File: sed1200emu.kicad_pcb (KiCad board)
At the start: 2 copper layers, 46.2 x 38.9 mm, 17 parts, among them IC1 MEGA8-AI

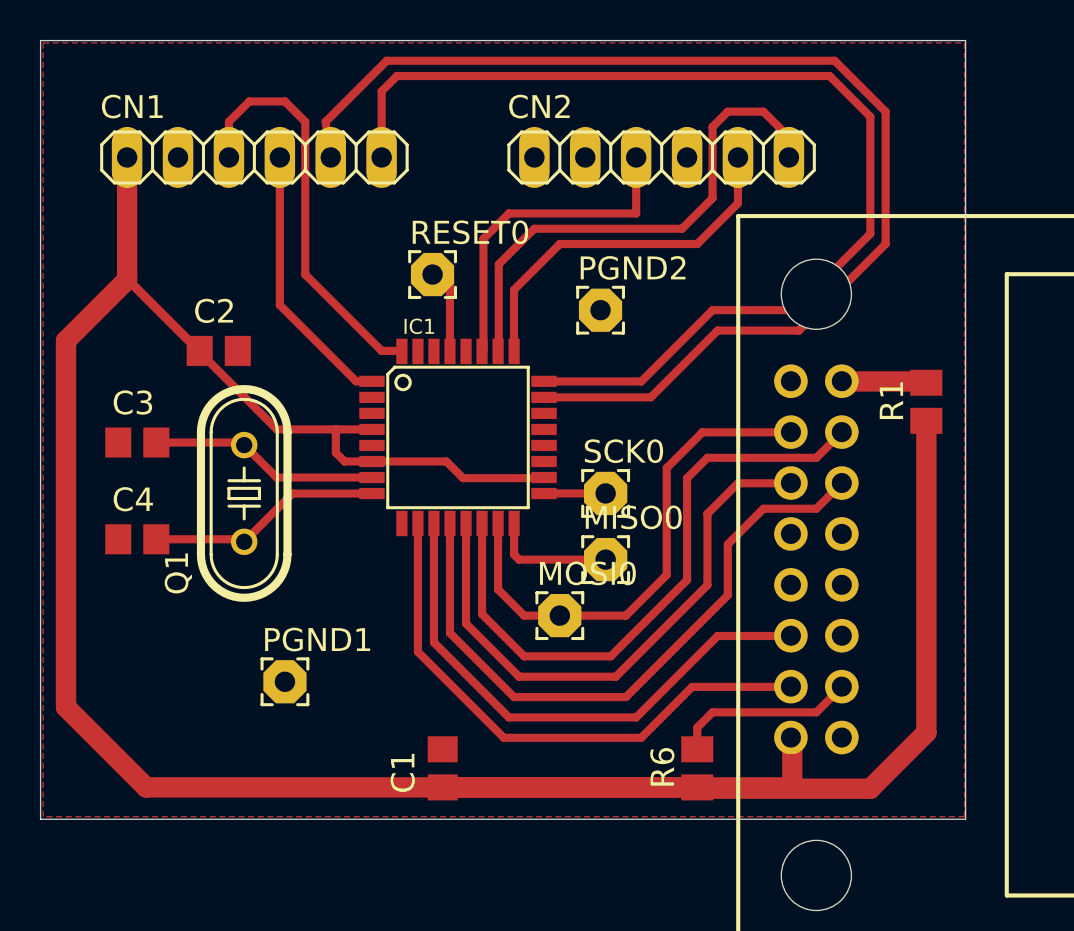
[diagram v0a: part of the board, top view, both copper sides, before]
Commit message: Replace MEGA8 Symbol and Footprint
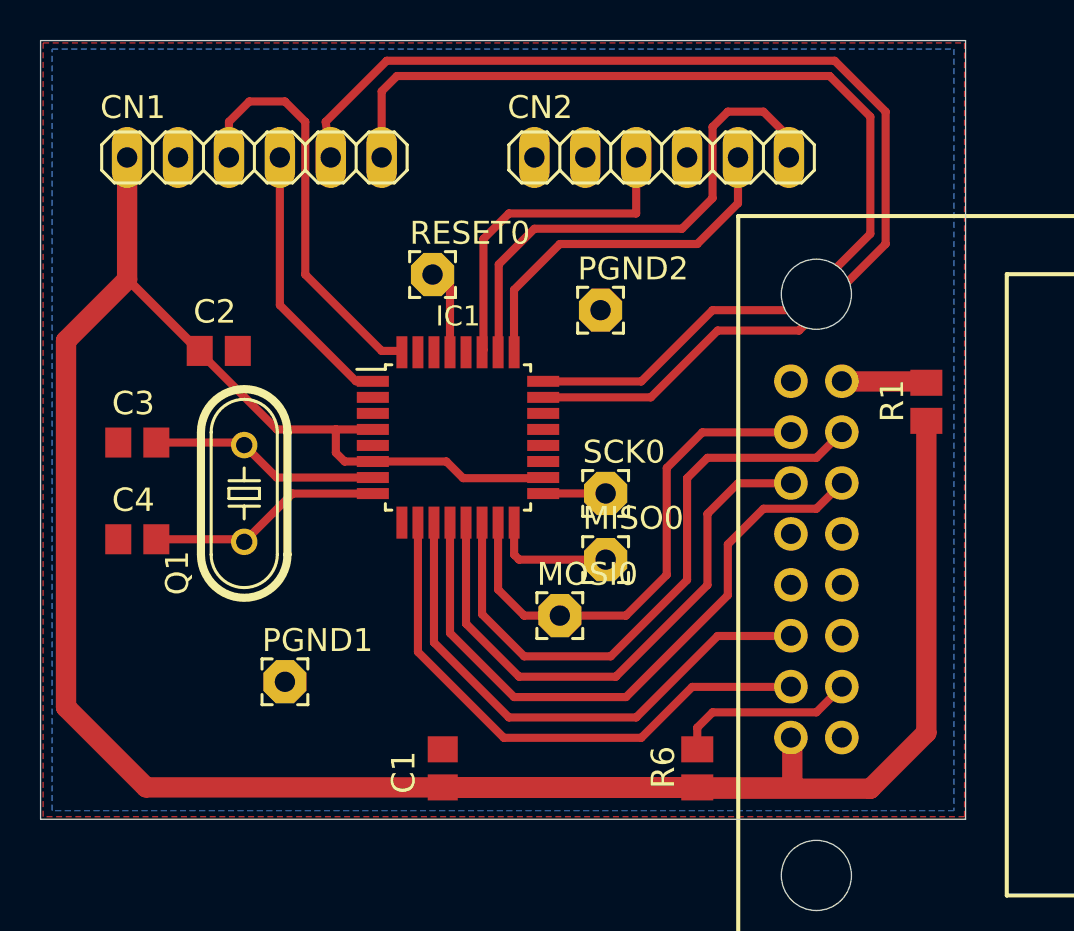
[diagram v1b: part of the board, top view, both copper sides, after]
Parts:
- CN1, CN2: value (none) -> PINHD-1X6
- IC1: footprint sed1200emu:TQFP32-08 -> Package_QFP:TQFP-32_7x7mm_P0.8mm
- PGND1, PGND2: value (none) -> 2,15/1,0
- Q1: value (none) -> CRYSTALHC49S
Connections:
- net PS2CLK renamed Net-(IC1-PD2(INT0))
- net PS2DATA renamed Net-(IC1-PD3(INT1))
- CN1 pad 2: (no net) -> unconnected-(CN1-Pad2)
- CN2 pad 2: (no net) -> unconnected-(CN2-Pad2)
- CN2 pad 4: (no net) -> unconnected-(CN2-Pad4)
- DIS2 pad 10: (no net) -> unconnected-(DIS2-D3-Pad10)
- DIS2 pad 15: N$7 -> unconnected-(DIS2-NC@1-Pad15)
- DIS2 pad 16: GND -> unconnected-(DIS2-NC@2-Pad16)
- DIS2 pad 7: (no net) -> unconnected-(DIS2-D0-Pad7)
- DIS2 pad 8: (no net) -> unconnected-(DIS2-D1-Pad8)
- DIS2 pad 9: (no net) -> unconnected-(DIS2-D2-Pad9)
- IC1 pad 19: (no net) -> unconnected-(IC1-ADC6-Pad19)
- IC1 pad 2: (no net) -> unconnected-(IC1-PD4(XCK/T0)-Pad2)
- IC1 pad 20: (no net) -> unconnected-(IC1-AREF-Pad20)
- IC1 pad 22: (no net) -> unconnected-(IC1-ADC7-Pad22)
- IC1 pad 28: (no net) -> unconnected-(IC1-PC5(ADC5/SCL)-Pad28)
- IC1 pad 30: (no net) -> unconnected-(IC1-PD0(RXD)-Pad30)
- IC1 pad 31: (no net) -> unconnected-(IC1-PD1(TXD)-Pad31)
- IC1 pad 9: (no net) -> unconnected-(IC1-PD5(T1)-Pad9)
- R1 pad 2: N$7 -> unconnected-(R1-Pad2)
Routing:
- net N$7: track 4.24 -> 0.00 mm
- net (no net): track 0.00 -> 4.24 mm
- added copper zone on B.Cu, net GND

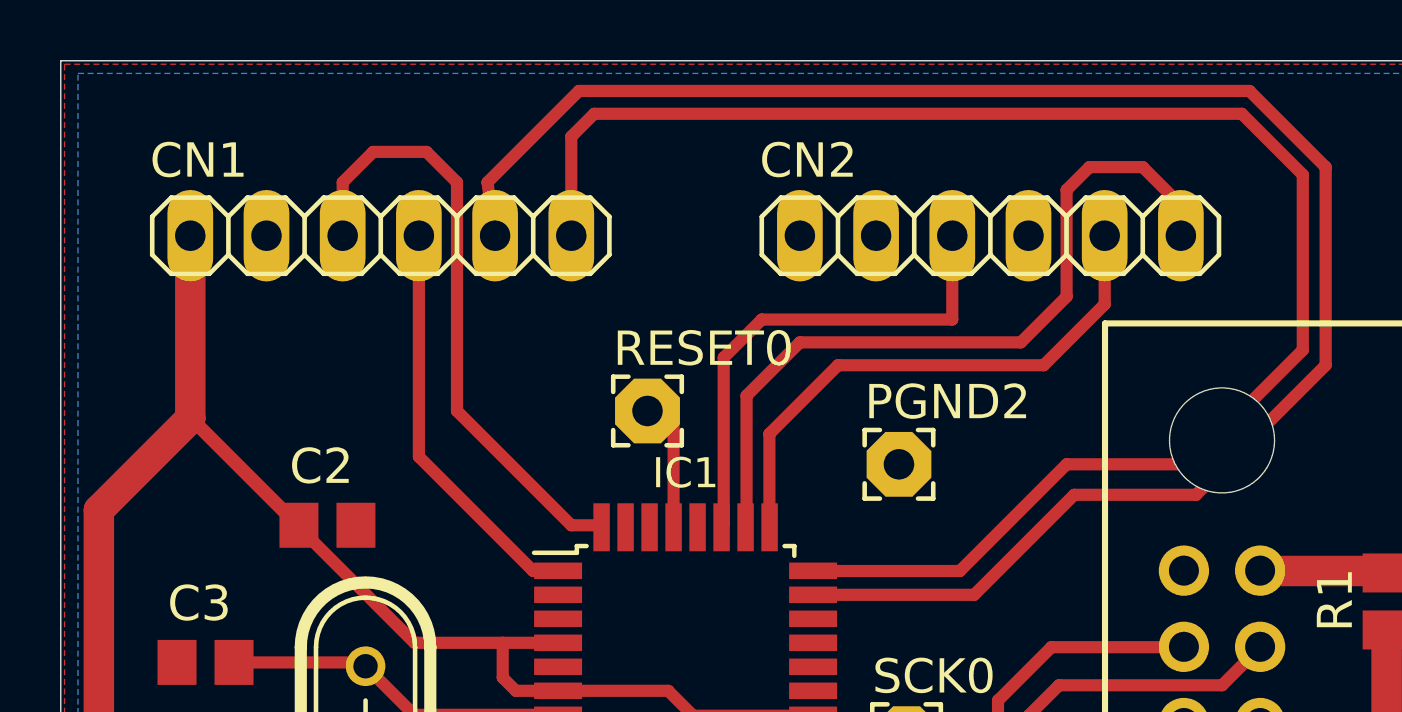
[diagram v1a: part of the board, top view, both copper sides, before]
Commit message: Replace CN1 and CN2 with KiCad Symbols
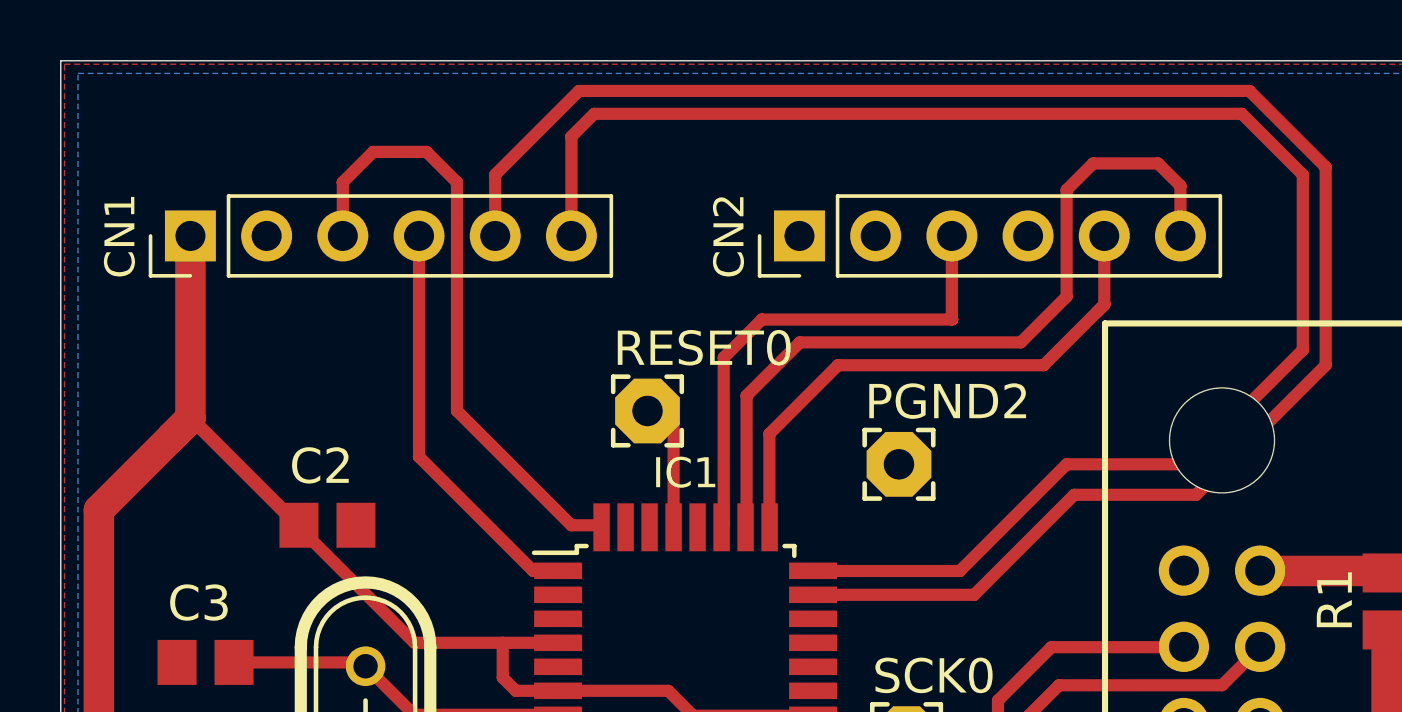
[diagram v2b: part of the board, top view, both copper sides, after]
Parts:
- CN1, CN2: footprint sed1200emu:1X06 -> Connector_PinHeader_2.54mm:PinHeader_1x06_P2.54mm_Vertical
- moved CN2 6.36 mm to (150.0, 91.4), turned to 90 degrees
- moved CN1 6.35 mm to (129.7, 91.4), turned to 90 degrees
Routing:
- net VCC: track 142.5 -> 143.3 mm

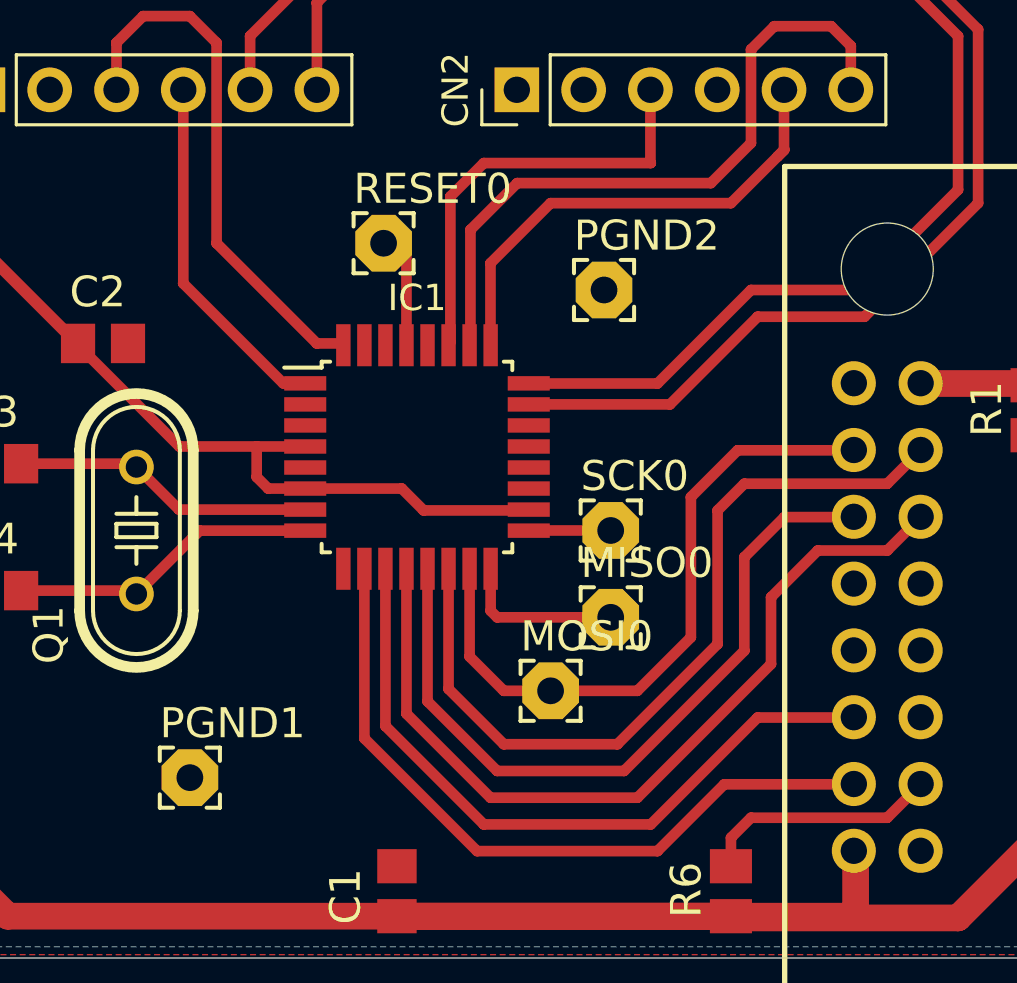
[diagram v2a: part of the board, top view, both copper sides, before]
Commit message: Replace all 1pin out headers to KiCad Symbols
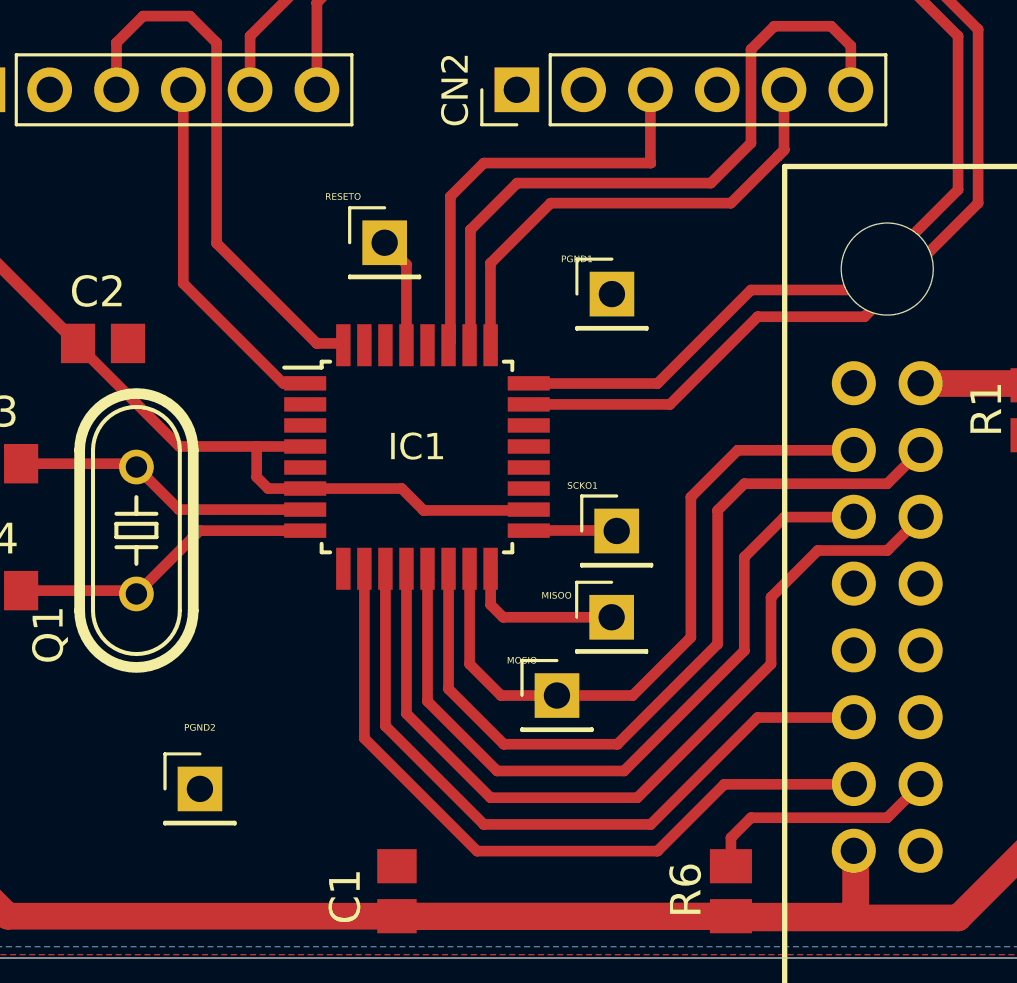
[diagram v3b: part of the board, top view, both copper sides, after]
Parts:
- removed MISO0: MISO, sed1200emu:2,15_1,0
- removed MOSI0: MOSI, sed1200emu:2,15_1,0
- removed RESET0: RESET, sed1200emu:2,15_1,0
- removed SCK0: SCK, sed1200emu:2,15_1,0
- added MISOO: Conn_01x01_Pin, Connector_PinHeader_2.54mm:PinHeader_1x01_P2.54mm_Vertical, F.Cu at (153.7, 111.5)
- added MOSIO: Conn_01x01_Pin, Connector_PinHeader_2.54mm:PinHeader_1x01_P2.54mm_Vertical, F.Cu at (151.6, 114.4)
- added RESETO: Conn_01x01_Pin, Connector_PinHeader_2.54mm:PinHeader_1x01_P2.54mm_Vertical, F.Cu at (145.0, 97.2)
- added SCKO1: Conn_01x01_Pin, Connector_PinHeader_2.54mm:PinHeader_1x01_P2.54mm_Vertical, F.Cu at (153.8, 108.2)
- PGND1, PGND2: value 2,15/1,0 -> Conn_01x01_Pin; footprint sed1200emu:2,15_1,0 -> Connector_PinHeader_2.54mm:PinHeader_1x01_P2.54mm_Vertical
- moved PGND2 24.4 mm to (138.0, 118.0)
- moved PGND1 24.4 mm to (153.7, 99.2)
